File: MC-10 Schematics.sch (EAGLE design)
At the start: 154 parts, among them IC2 MC1372, J4 22-27-2081-08, J5 22-27-2081-08, Q1 2SC1674, T102 71K1-2-4, U1 MC6803, U10 uPD4016, U11 MC6847, U12 74LS14N, U13 74LS32N, U14 MC14503B, U15 LM339N, U16 LM741P, U18 74LS74N, U19 7476N, U2 74LS373N, U20 74LS32N, U3 TMS2564, U4 74LS155N, U5 74LS367N, U6 74LS367N, U7 74LS245N, U8 74LS174N, U9 uPD4016, X1 RF Out, X101 3.579545

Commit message: RevA of schematics, corrected edge connector on library
Rev A: /OE from SRAMs connected to GND, Selection signal names according to MC-10 service manual, Corrected opamp rails to +/-10V, deleted unused gates.
Added blank positions on the edge connectors (equivalent to pins 35, 36)
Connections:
- net !KBD renamed !KEYRD
- net !VDG_MODE renamed !VDG_CTL
- net !VRAM_CS renamed !MS
- net !VRAM_RD renamed !R!/W
- net !VRAM_WR renamed !MW
- net +12V renamed +10V
- net -12V renamed -10V
- net CPU_CLOCK renamed !WIN
- net GND: now also U10G$1.!OE, U9G$1.!OE
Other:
- note added: "(CPU Clock)"
- note added: "Rev a: /OE from SRAMs connected to GND, Selection signal names according to MC-10 service manual, Corrected opamp rails to +/-10V, deleted unused gates"
- note removed: "-"
- moved on the sheet: C22, U14, U7, U8

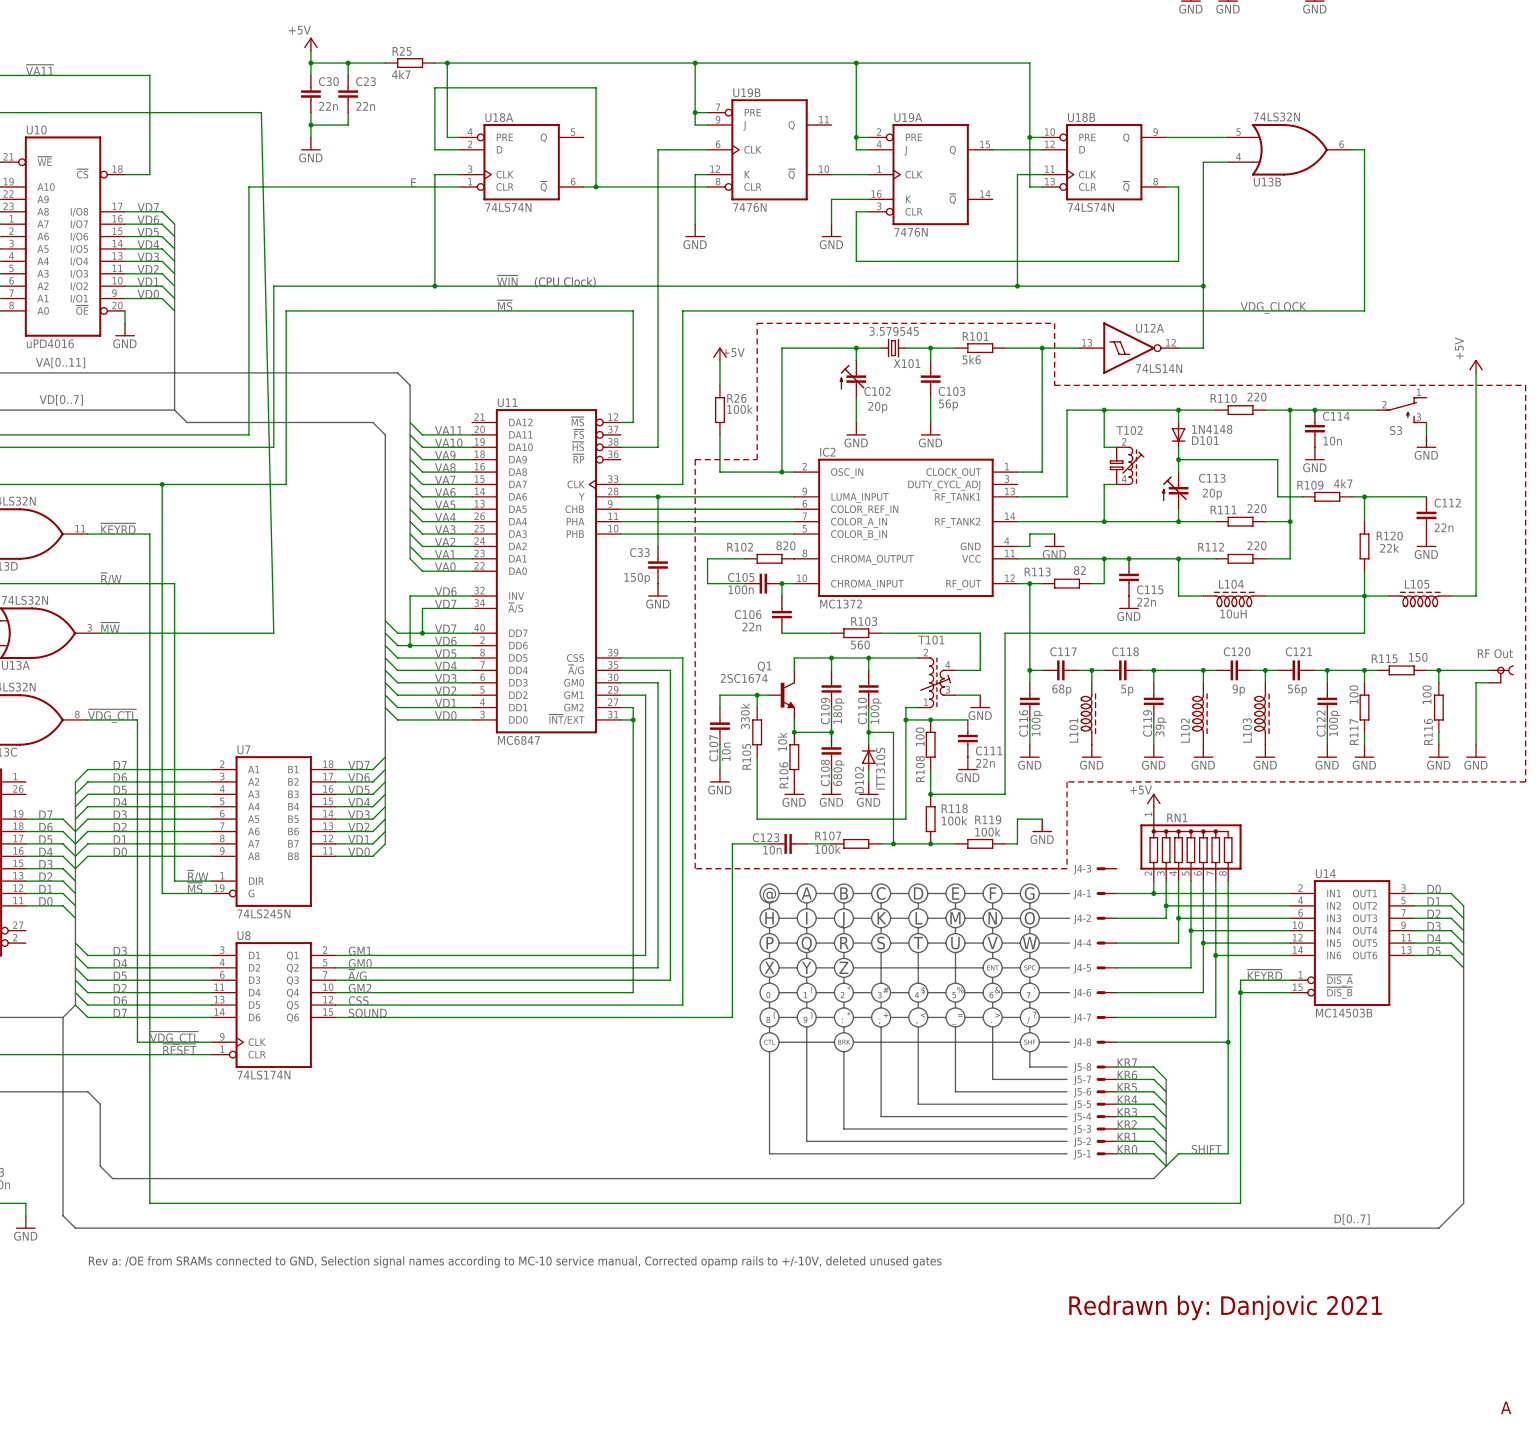
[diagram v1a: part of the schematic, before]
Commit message: Corrected connection of 3.579545 MHz CLK and /WIN signal
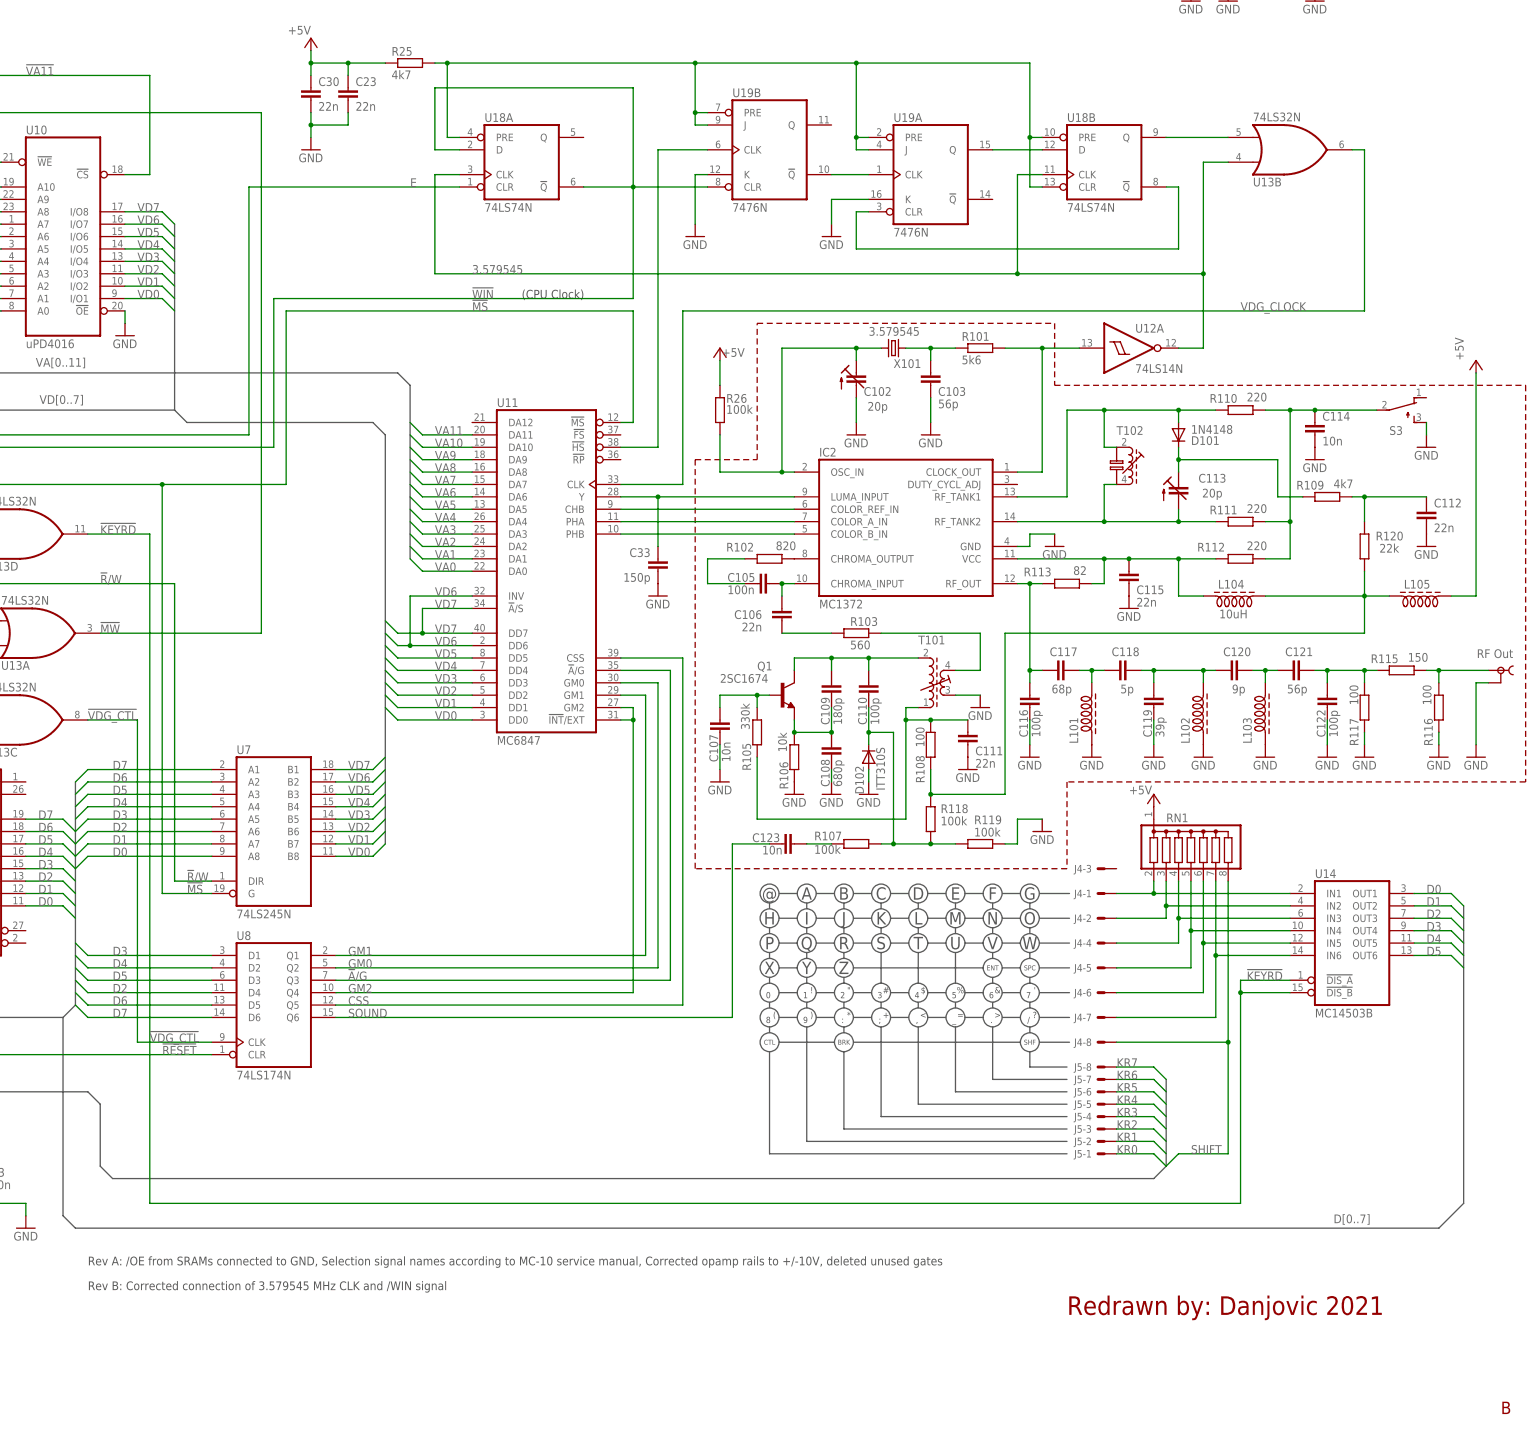
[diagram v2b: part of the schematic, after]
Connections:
- removed net N$11: U18A.!Q, U18A.D, U19B.CLR
- new net 3.579545: U12A.O, U13B.I0, U18A.CLK, U18B.CLK
- net !WIN: now also U18A.!Q, U18A.D, U19B.CLR; no longer U12A.O, U13B.I0, U18A.CLK, U18B.CLK
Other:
- note added: "Rev A: /OE from SRAMs connected to GND, Selection signal names according to MC-10 service manual, Corrected opamp rails to +/-10V, deleted unused gates"
- note added: "Rev B: Corrected connection of 3.579545 MHz CLK and /WIN signal"
- note removed: "Rev a: /OE from SRAMs connected to GND, Selection signal names according to MC-10 service manual, Corrected opamp rails to +/-10V, deleted unused gates"
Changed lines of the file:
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@@
 <text x="-22.86" y="259.08" size="1.778" layer="97">CASSETE</text>
 <text x="144.78" y="-30.48" size="3.81" layer="94" font="vector" ratio="12">Redrawn by: Danjovic 2021</text>
-<text x="233.68" y="-50.8" size="2.54" layer="94" font="vector" ratio="12">A</text>
+<text x="233.68" y="-50.8" size="2.54" layer="94" font="vector" ratio="12">B</text>
 <text x="218.44" y="269.24" size="1.778" layer="97">8 Vac</text>
-<text x="-55.88" y="-20.32" size="1.778" layer="97">Rev a: /OE from SRAMs connected to GND, Selection signal names according to MC-10 service manual, Corrected opamp rails to +/-10V, deleted unused gates</text>
-<text x="35.56" y="180.34" size="1.778" layer="97">(CPU Clock)</text>
+<text x="-55.88" y="-20.32" size="1.778" layer="97">Rev A: /OE from SRAMs connected to GND, Selection signal names according to MC-10 service manual, Corrected opamp rails to +/-10V, deleted unused gates</text>
+<text x="33.02" y="177.8" size="1.778" layer="97">(CPU Clock)</text>
 <text x="-170.18" y="147.32" size="1.778" layer="97">(CPU Clock)</text>
 <text x="-241.3" y="127" size="1.778" layer="97">(CPU Clock)</text>
+<text x="-55.88" y="-25.4" size="1.778" layer="97">Rev B: Corrected connection of 3.579545 MHz CLK and /WIN signal</text>
 </plain>
 <instances>
@@
 <junction x="-190.5" y="165.1"/>
 <junction x="-190.5" y="203.2"/>
-<label x="27.94" y="175.26" size="1.778" layer="95"/>
+<label x="22.86" y="175.26" size="1.778" layer="95"/>
 <pinref part="U7" gate="A" pin="G"/>
 <wire x1="-30.48" y1="55.88" x2="-40.64" y2="55.88" width="0.1524" layer="91"/>
@@
 <segment>
 <pinref part="U13" gate="A" pin="O"/>
-<wire x1="-17.78" y1="109.22" x2="-53.34" y2="109.22" width="0.1524" layer="91"/>
+<wire x1="-20.32" y1="109.22" x2="-53.34" y2="109.22" width="0.1524" layer="91"/>
 <label x="-53.34" y="109.22" size="1.778" layer="95"/>
 <pinref part="U9" gate="G$1" pin="!WE"/>
@@
 <wire x1="-142.24" y1="215.9" x2="-86.36" y2="215.9" width="0.1524" layer="91"/>
 <wire x1="-86.36" y1="215.9" x2="-20.32" y2="215.9" width="0.1524" layer="91"/>
-<wire x1="-20.32" y1="215.9" x2="-17.78" y2="109.22" width="0.1524" layer="91"/>
+<wire x1="-20.32" y1="215.9" x2="-20.32" y2="109.22" width="0.1524" layer="91"/>
 <pinref part="U10" gate="G$1" pin="!WE"/>
 <wire x1="-73.66" y1="205.74" x2="-86.36" y2="205.74" width="0.1524" layer="91"/>
@@
 </segment>
 </net>
-<net name="N$11" class="0">
-<segment>
-<pinref part="U18" gate="A" pin="D"/>
-<wire x1="20.32" y1="208.28" x2="15.24" y2="208.28" width="0.1524" layer="91"/>
-<wire x1="15.24" y1="208.28" x2="15.24" y2="220.98" width="0.1524" layer="91"/>
-<wire x1="15.24" y1="220.98" x2="48.26" y2="220.98" width="0.1524" layer="91"/>
-<wire x1="48.26" y1="220.98" x2="48.26" y2="200.66" width="0.1524" layer="91"/>
-<pinref part="U18" gate="A" pin="!Q"/>
-<wire x1="48.26" y1="200.66" x2="45.72" y2="200.66" width="0.1524" layer="91"/>
-<pinref part="U19" gate="B" pin="CLR"/>
-<wire x1="71.12" y1="200.66" x2="48.26" y2="200.66" width="0.1524" layer="91"/>
-<junction x="48.26" y="200.66"/>
-</segment>
-</net>
 <net name="N$10" class="0">
 <segment>
 <pinref part="U19" gate="A" pin="CLR"/>
 <wire x1="104.14" y1="195.58" x2="101.6" y2="195.58" width="0.1524" layer="91"/>
-<wire x1="101.6" y1="195.58" x2="101.6" y2="185.42" width="0.1524" layer="91"/>
-<wire x1="101.6" y1="185.42" x2="167.64" y2="185.42" width="0.1524" layer="91"/>
-<wire x1="167.64" y1="185.42" x2="167.64" y2="200.66" width="0.1524" layer="91"/>
+<wire x1="101.6" y1="195.58" x2="101.6" y2="187.96" width="0.1524" layer="91"/>
+<wire x1="101.6" y1="187.96" x2="167.64" y2="187.96" width="0.1524" layer="91"/>
+<wire x1="167.64" y1="187.96" x2="167.64" y2="200.66" width="0.1524" layer="91"/>
 <pinref part="U18" gate="B" pin="!Q"/>
 <wire x1="167.64" y1="200.66" x2="165.1" y2="200.66" width="0.1524" layer="91"/>
@@
 <wire x1="-203.2" y1="127" x2="-203.2" y2="147.32" width="0.1524" layer="91"/>
 <wire x1="-203.2" y1="147.32" x2="-17.78" y2="147.32" width="0.1524" layer="91"/>
-<wire x1="-17.78" y1="147.32" x2="-17.78" y2="180.34" width="0.1524" layer="91"/>
-<pinref part="U18" gate="A" pin="CLK"/>
-<wire x1="20.32" y1="203.2" x2="15.24" y2="203.2" width="0.1524" layer="91"/>
-<wire x1="15.24" y1="203.2" x2="15.24" y2="180.34" width="0.1524" layer="91"/>
-<wire x1="15.24" y1="180.34" x2="134.62" y2="180.34" width="0.1524" layer="91"/>
-<pinref part="U18" gate="B" pin="CLK"/>
-<wire x1="139.7" y1="203.2" x2="134.62" y2="203.2" width="0.1524" layer="91"/>
-<wire x1="134.62" y1="203.2" x2="134.62" y2="180.34" width="0.1524" layer="91"/>
-<wire x1="134.62" y1="180.34" x2="172.72" y2="180.34" width="0.1524" layer="91"/>
-<junction x="134.62" y="180.34"/>
-<wire x1="172.72" y1="180.34" x2="172.72" y2="205.74" width="0.1524" layer="91"/>
-<pinref part="U13" gate="B" pin="I0"/>
-<wire x1="172.72" y1="205.74" x2="177.8" y2="205.74" width="0.1524" layer="91"/>
-<wire x1="-17.78" y1="180.34" x2="15.24" y2="180.34" width="0.1524" layer="91"/>
-<junction x="15.24" y="180.34"/>
-<label x="27.94" y="180.34" size="1.778" layer="95"/>
+<wire x1="-17.78" y1="147.32" x2="-17.78" y2="177.8" width="0.1524" layer="91"/>
+<wire x1="-17.78" y1="177.8" x2="55.88" y2="177.8" width="0.1524" layer="91"/>
+<wire x1="55.88" y1="177.8" x2="55.88" y2="200.66" width="0.1524" layer="91"/>
+<label x="22.86" y="177.8" size="1.778" layer="95"/>
 <label x="-248.92" y="127" size="1.778" layer="95"/>
 <label x="-177.8" y="147.32" size="1.778" layer="95"/>
-<wire x1="172.72" y1="180.34" x2="172.72" y2="167.64" width="0.1524" layer="91"/>
-<junction x="172.72" y="180.34"/>
-<pinref part="U12" gate="A" pin="O"/>
-<wire x1="172.72" y1="167.64" x2="167.64" y2="167.64" width="0.1524" layer="91"/>
+<pinref part="U18" gate="A" pin="D"/>
+<wire x1="20.32" y1="208.28" x2="15.24" y2="208.28" width="0.1524" layer="91"/>
+<wire x1="15.24" y1="208.28" x2="15.24" y2="220.98" width="0.1524" layer="91"/>
+<wire x1="15.24" y1="220.98" x2="55.88" y2="220.98" width="0.1524" layer="91"/>
+<wire x1="55.88" y1="220.98" x2="55.88" y2="200.66" width="0.1524" layer="91"/>
+<pinref part="U18" gate="A" pin="!Q"/>
+<wire x1="55.88" y1="200.66" x2="45.72" y2="200.66" width="0.1524" layer="91"/>
+<pinref part="U19" gate="B" pin="CLR"/>
+<wire x1="71.12" y1="200.66" x2="55.88" y2="200.66" width="0.1524" layer="91"/>
+<junction x="55.88" y="200.66"/>
 </segment>
 </net>
@@
 </segment>
 </net>
+<net name="3.579545" class="0">
+<segment>
+<pinref part="U12" gate="A" pin="O"/>
+<wire x1="172.72" y1="167.64" x2="167.64" y2="167.64" width="0.1524" layer="91"/>
+<pinref part="U13" gate="B" pin="I0"/>
+<wire x1="172.72" y1="205.74" x2="177.8" y2="205.74" width="0.1524" layer="91"/>
+<wire x1="172.72" y1="182.88" x2="172.72" y2="205.74" width="0.1524" layer="91"/>
+<wire x1="172.72" y1="182.88" x2="172.72" y2="167.64" width="0.1524" layer="91"/>
+<junction x="172.72" y="182.88"/>
+<wire x1="134.62" y1="182.88" x2="172.72" y2="182.88" width="0.1524" layer="91"/>
+<pinref part="U18" gate="B" pin="CLK"/>
+<wire x1="139.7" y1="203.2" x2="134.62" y2="203.2" width="0.1524" layer="91"/>
+<wire x1="134.62" y1="203.2" x2="134.62" y2="182.88" width="0.1524" layer="91"/>
+<junction x="134.62" y="182.88"/>
+<pinref part="U18" gate="A" pin="CLK"/>
+<wire x1="20.32" y1="203.2" x2="15.24" y2="203.2" width="0.1524" layer="91"/>
+<wire x1="15.24" y1="203.2" x2="15.24" y2="182.88" width="0.1524" layer="91"/>
+<wire x1="15.24" y1="182.88" x2="134.62" y2="182.88" width="0.1524" layer="91"/>
+<label x="22.86" y="182.88" size="1.778" layer="95"/>
+</segment>
+</net>

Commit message: Further Correction on of 3.579545 MHz CLK and /WIN signal
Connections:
- net !WIN: now also U4A.2C; no longer U1.EXTAL2
- net 3.579545: now also U1.EXTAL2
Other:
- moved on the sheet: R21, U12C, U12F, U13A, U13C, U13D, U20A, U4

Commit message: Schematics update, Added AV Mod schematics
Schematics Rev C: Updated DIN connectors, added pinout on RF modulator, added Test Points
Added Schematics for Audio-Video Mod (RF modulator replacement)
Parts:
- added GND, TP1, TP2: TPPAD1-13, testpad:TPPAD1-13
- J1: device con-yamaichi:MD05SS -> MC-10:DS-4-05
- J2: device con-yamaichi:MD04SS -> MC-10:DS-4-04
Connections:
- net +5V: now also TP1.TP
- net GND: now also GND.TP
- net VDG_CLOCK: now also TP2.TP
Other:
- note added: "(1)"
- note added: "(2)"
- note added: "(3)"
- note added: "(4)"
- note added: "(5)"
- note added: "(6)"
- note added: "(7)"
- note added: "(8)"
- note added: "(9)"
- note added: "Rev C: Updated DIN connectors, added pinout on RF modulator, added Test Points"
- moved on the sheet: S3

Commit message: schematics and library update
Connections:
- net +5V: now also U3A..VCC, U3A.VPP
- net GND: now also U3A.!CS1, U3A.!CS2
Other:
- note added: "Rev D: Corrected 6803 SC1/SC2 pinout (thanks Brendan), added missing GND connection to both ROM /CS pins, added missing VCC power connection on ROM"
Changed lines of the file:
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@@
 <part name="TP2" library="testpad" deviceset="TP" device="PAD1-13"/>
 <part name="GND" library="testpad" deviceset="TP" device="PAD1-13"/>
+<part name="GND60" library="supply1" deviceset="GND" device=""/>
+<part name="P+9" library="supply1" deviceset="+5V" device=""/>
 </parts>
 <sheets>
@@
 <text x="-25.4" y="261.62" size="1.778" layer="97">CASSETE</text>
 <text x="144.78" y="-30.48" size="3.81" layer="94" font="vector" ratio="12">Redrawn by: Danjovic 2021</text>
-<text x="233.68" y="-50.8" size="2.54" layer="94" font="vector" ratio="12">C</text>
+<text x="233.68" y="-50.8" size="2.54" layer="94" font="vector" ratio="12">D</text>
 <text x="218.44" y="269.24" size="1.778" layer="97">8 Vac</text>
 <text x="-55.88" y="-20.32" size="1.778" layer="97">Rev A: /OE from SRAMs connected to GND, Selection signal names according to MC-10 service manual, Corrected opamp rails to +/-10V, deleted unused gates</text>
@@
 <text x="226.06" y="158.242" size="1.27" layer="97">(8)</text>
 <text x="210.82" y="158.242" size="1.27" layer="97">(9)</text>
+<text x="-55.88" y="-35.56" size="1.778" layer="97">Rev D: Corrected 6803 SC1/SC2 pinout (thanks Brendan), added missing GND connection to both ROM /CS pins, added missing VCC power connection on ROM </text>
 </plain>
 <instances>
@@
 <instance part="TP2" gate="G$1" x="60.96" y="142.24"/>
 <instance part="GND" gate="G$1" x="81.28" y="320.04" rot="R180"/>
+<instance part="GND60" gate="1" x="-66.04" y="40.64"/>
+<instance part="P+9" gate="1" x="-66.04" y="83.82" smashed="yes">
+<attribute name="VALUE" x="-68.58" y="83.82" size="1.778" layer="96" rot="R180"/>
+</instance>
 </instances>
 <busses>
@@
 <wire x1="81.28" y1="345.44" x2="81.28" y2="342.9" width="0.1524" layer="91"/>
 </segment>
+<segment>
+<pinref part="U3" gate="A" pin=".VCC"/>
+<pinref part="P+9" gate="1" pin="+5V"/>
+<wire x1="-68.58" y1="76.2" x2="-66.04" y2="76.2" width="0.1524" layer="91"/>
+<wire x1="-66.04" y1="76.2" x2="-66.04" y2="78.74" width="0.1524" layer="91"/>
+<pinref part="U3" gate="A" pin="VPP"/>
+<wire x1="-66.04" y1="78.74" x2="-66.04" y2="81.28" width="0.1524" layer="91"/>
+<wire x1="-68.58" y1="78.74" x2="-66.04" y2="78.74" width="0.1524" layer="91"/>
+<junction x="-66.04" y="78.74"/>
+</segment>
 </net>
 <net name="RST_SW" class="0">
@@
 <wire x1="-48.26" y1="175.26" x2="-48.26" y2="172.72" width="0.1524" layer="91"/>
 </segment>
+<segment>
+<pinref part="U3" gate="A" pin="!CS2"/>
+<pinref part="GND60" gate="1" pin="GND"/>
+<wire x1="-68.58" y1="48.26" x2="-66.04" y2="48.26" width="0.1524" layer="91"/>
+<wire x1="-66.04" y1="48.26" x2="-66.04" y2="45.72" width="0.1524" layer="91"/>
+<pinref part="U3" gate="A" pin="!CS1"/>
+<wire x1="-66.04" y1="45.72" x2="-66.04" y2="43.18" width="0.1524" layer="91"/>
+<wire x1="-68.58" y1="45.72" x2="-66.04" y2="45.72" width="0.1524" layer="91"/>
+<junction x="-66.04" y="45.72"/>
+</segment>
 </net>
